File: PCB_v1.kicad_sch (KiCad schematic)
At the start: 38 parts

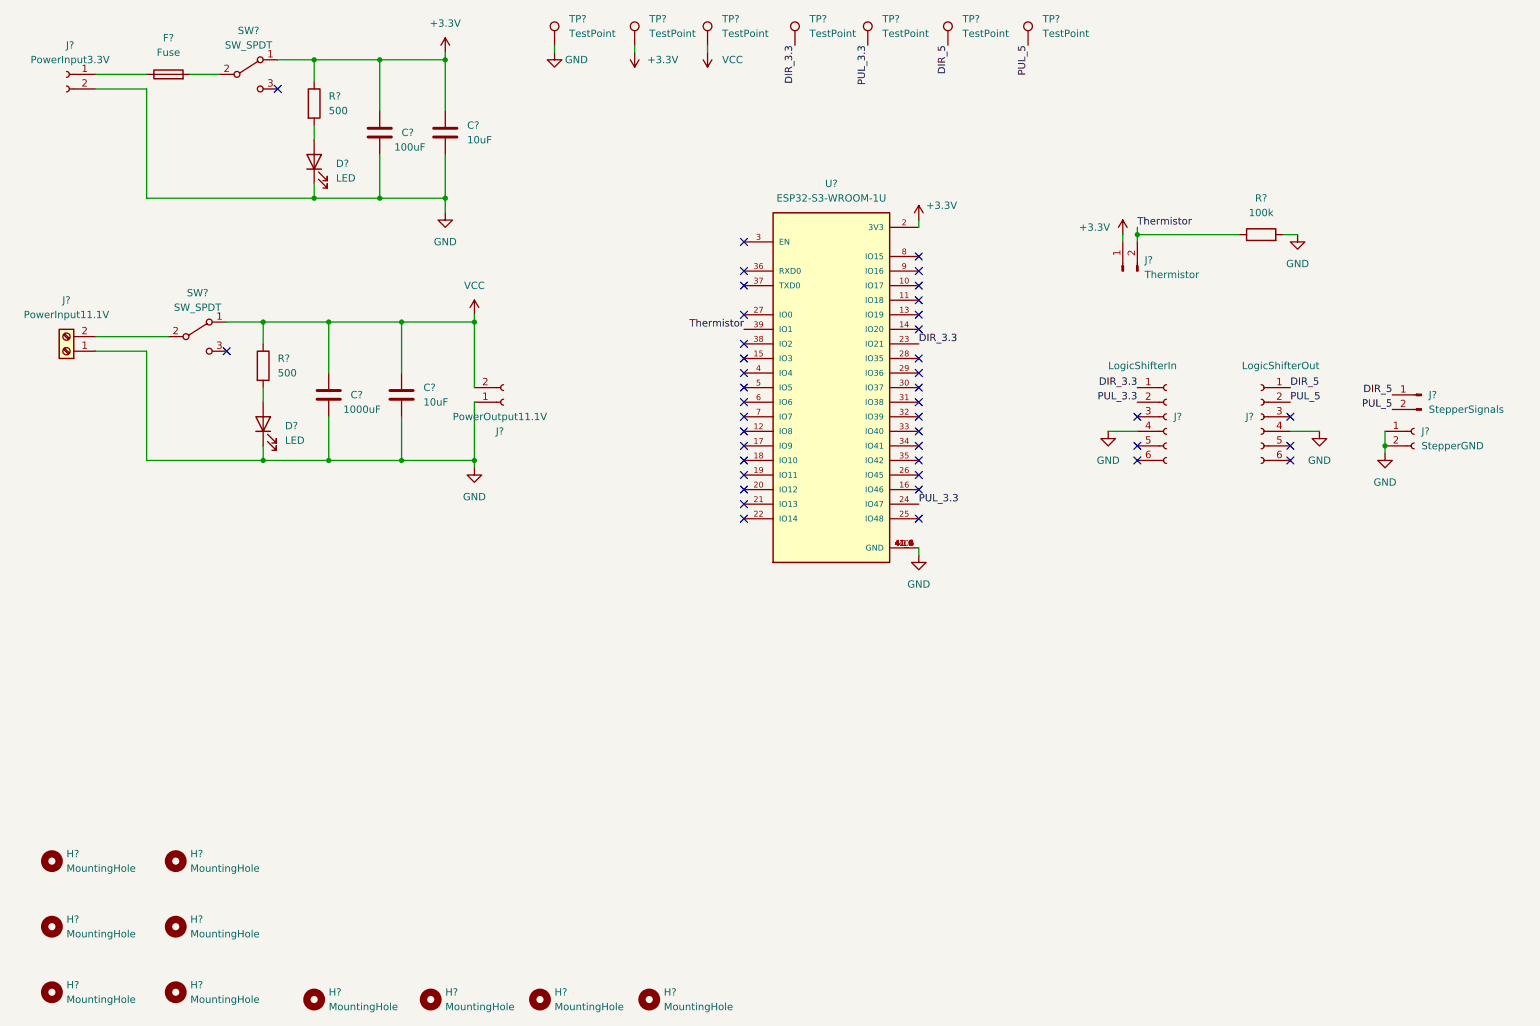
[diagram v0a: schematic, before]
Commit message: added footprints and layout
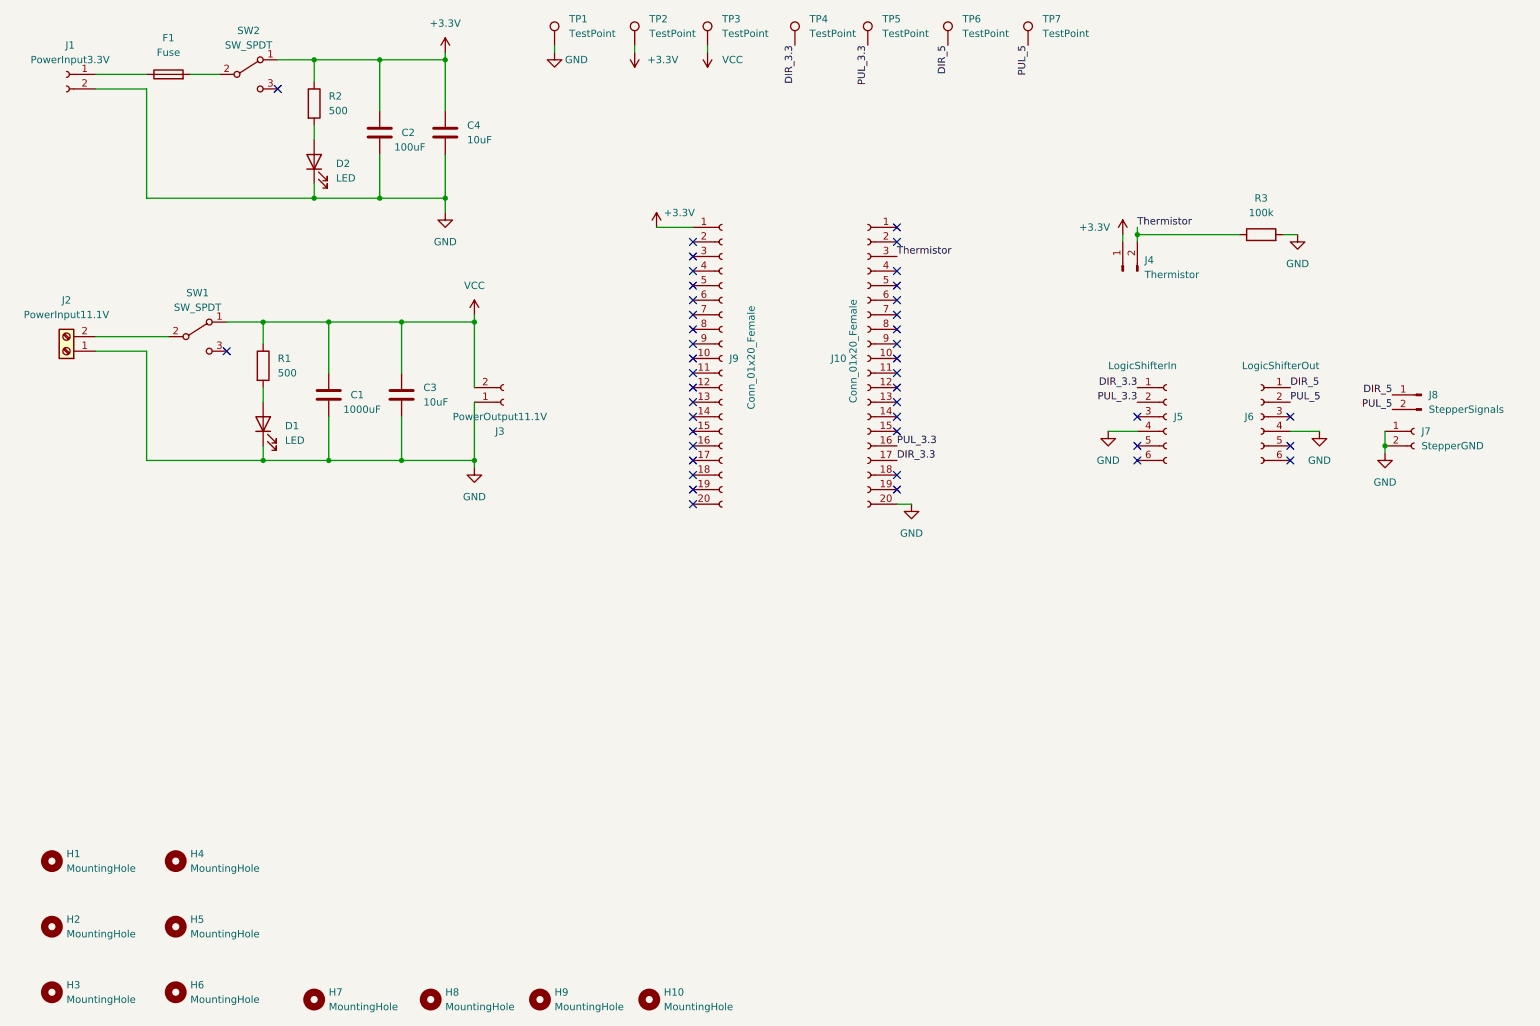
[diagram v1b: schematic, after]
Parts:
- removed U?: ESP32-S3-WROOM-1U, ESP32-S3-WROOM-1U:XCVR_ESP32-S3-WROOM-1U, symbol ESP32-S3-WROOM-1U:ESP32-S3-WROOM-1U
- added J10, J9: Conn_01x20_Female, Connector_PinSocket_2.54mm:PinSocket_1x20_P2.54mm_Vertical, symbol Connector:Conn_01x20_Female
- H1, H10, H2, H3, H4, H5, H6, H7, H8, H9: renamed from H?; footprint (none) -> MountingHole:MountingHole_3.2mm_M3
- J1, J3, J7: renamed from J?; footprint (none) -> Connector_PinSocket_2.54mm:PinSocket_1x02_P2.54mm_Vertical
- J2: renamed from J?; footprint (none) -> TerminalBlock:TerminalBlock_bornier-2_P5.08mm
- J4, J8: renamed from J?; footprint (none) -> Connector_PinHeader_2.54mm:PinHeader_1x02_P2.54mm_Vertical
- J5, J6: renamed from J?; footprint (none) -> Connector_PinSocket_2.54mm:PinSocket_1x06_P2.54mm_Vertical
- R3: renamed from R?; footprint (none) -> Resistor_THT:R_Axial_DIN0204_L3.6mm_D1.6mm_P2.54mm_Vertical
- TP1, TP2, TP3, TP4, TP5, TP6, TP7: renamed from TP?; footprint (none) -> Connector_PinHeader_2.54mm:PinHeader_1x01_P2.54mm_Vertical
- gave numbers to parts that had none: 11
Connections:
- net +3.3V: now also J9.1 (Pin_1)
- net DIR_3.3: now also J10.17 (Pin_17)
- net GND: now also J10.20 (Pin_20)
- net PUL_3.3: now also J10.16 (Pin_16)
- net Thermistor: now also J10.3 (Pin_3)
- no-connect marks 42 -> 43
